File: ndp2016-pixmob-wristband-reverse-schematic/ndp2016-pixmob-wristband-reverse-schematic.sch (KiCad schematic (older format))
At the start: 18 parts, among them IC1 AT24C02S, IC2 MC81F4204_V/M/R, SW1 Single-Axis Accelerometer, U1 IR

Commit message: schematic
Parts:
- SW1: value Single-Axis Accelerometer -> Accelerometer
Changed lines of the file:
@@
 encoding utf-8
 Sheet 1 1
-Title ""
-Date ""
-Rev ""
+Title "NDP2016 Pixmob Wristband Reverse Engineered"
+Date "2016-08-10"
+Rev "1"
 Comp ""
 Comment1 ""
@@
 P 8850 4600
 F 0 "SW1" H 8850 4700 50  0000 C CNN
-F 1 "Single-Axis Accelerometer" H 8850 4500 50  0000 C CNN
+F 1 "Accelerometer" H 8850 4500 50  0000 C CNN
 F 2 "" H 8850 4600 50  0000 C CNN
 F 3 "" H 8850 4600 50  0000 C CNN

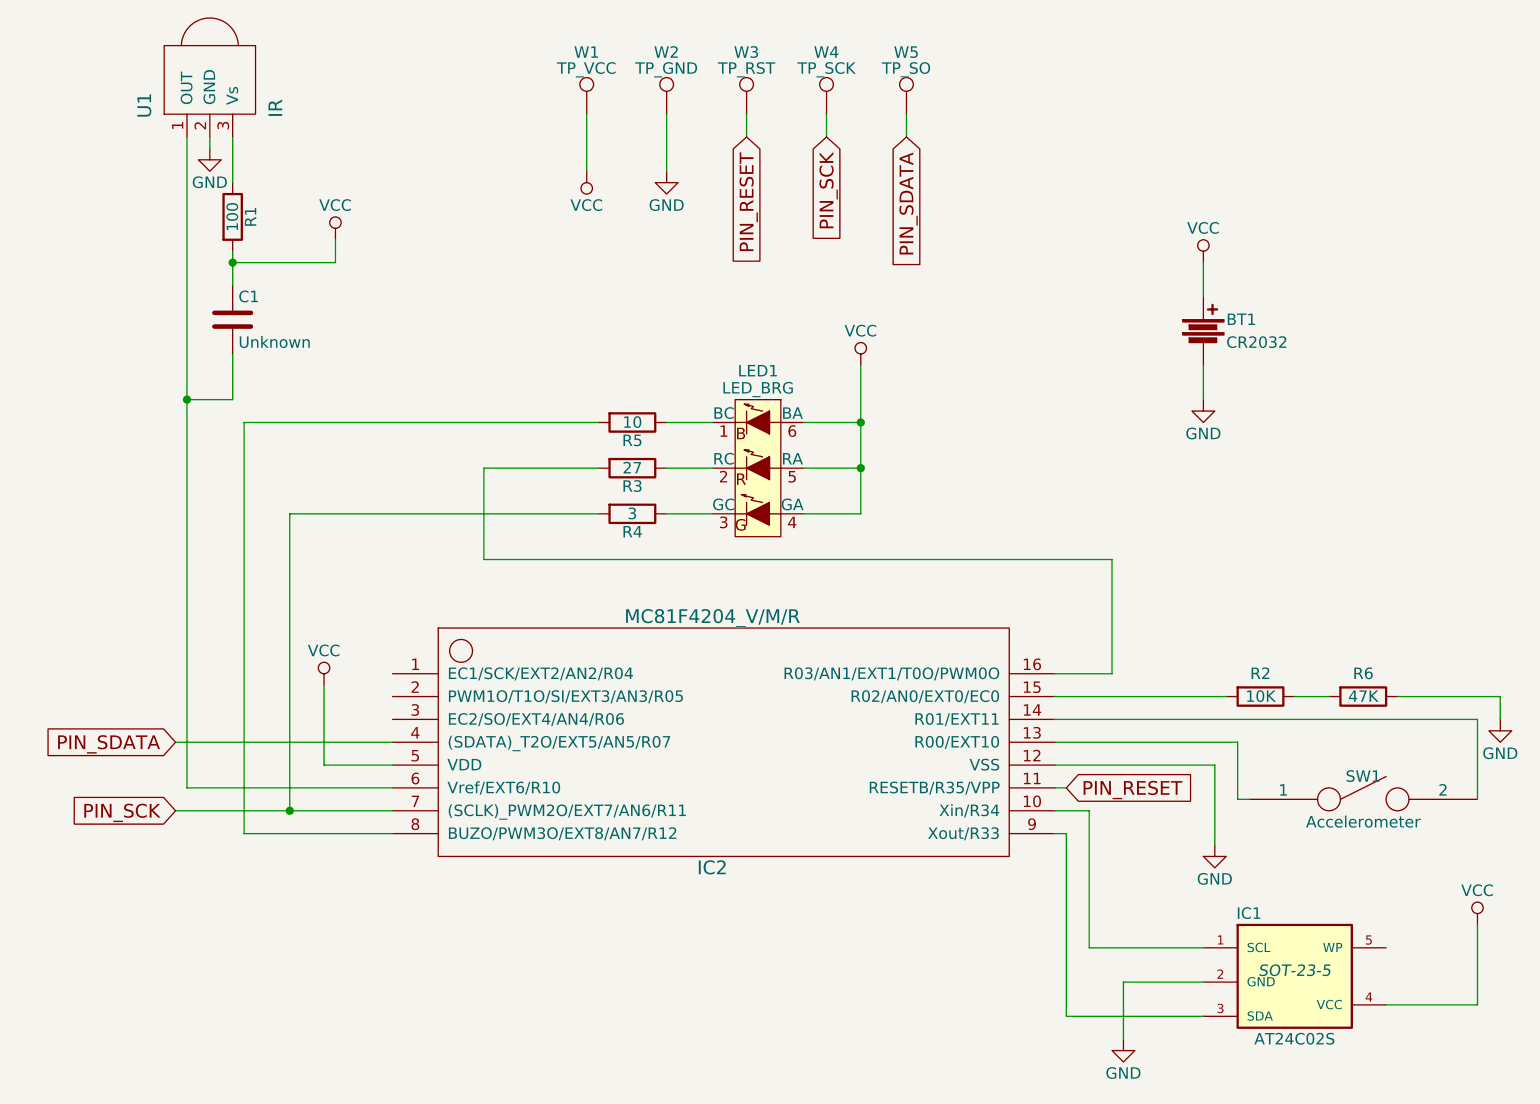
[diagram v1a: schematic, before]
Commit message: adjust cap ground
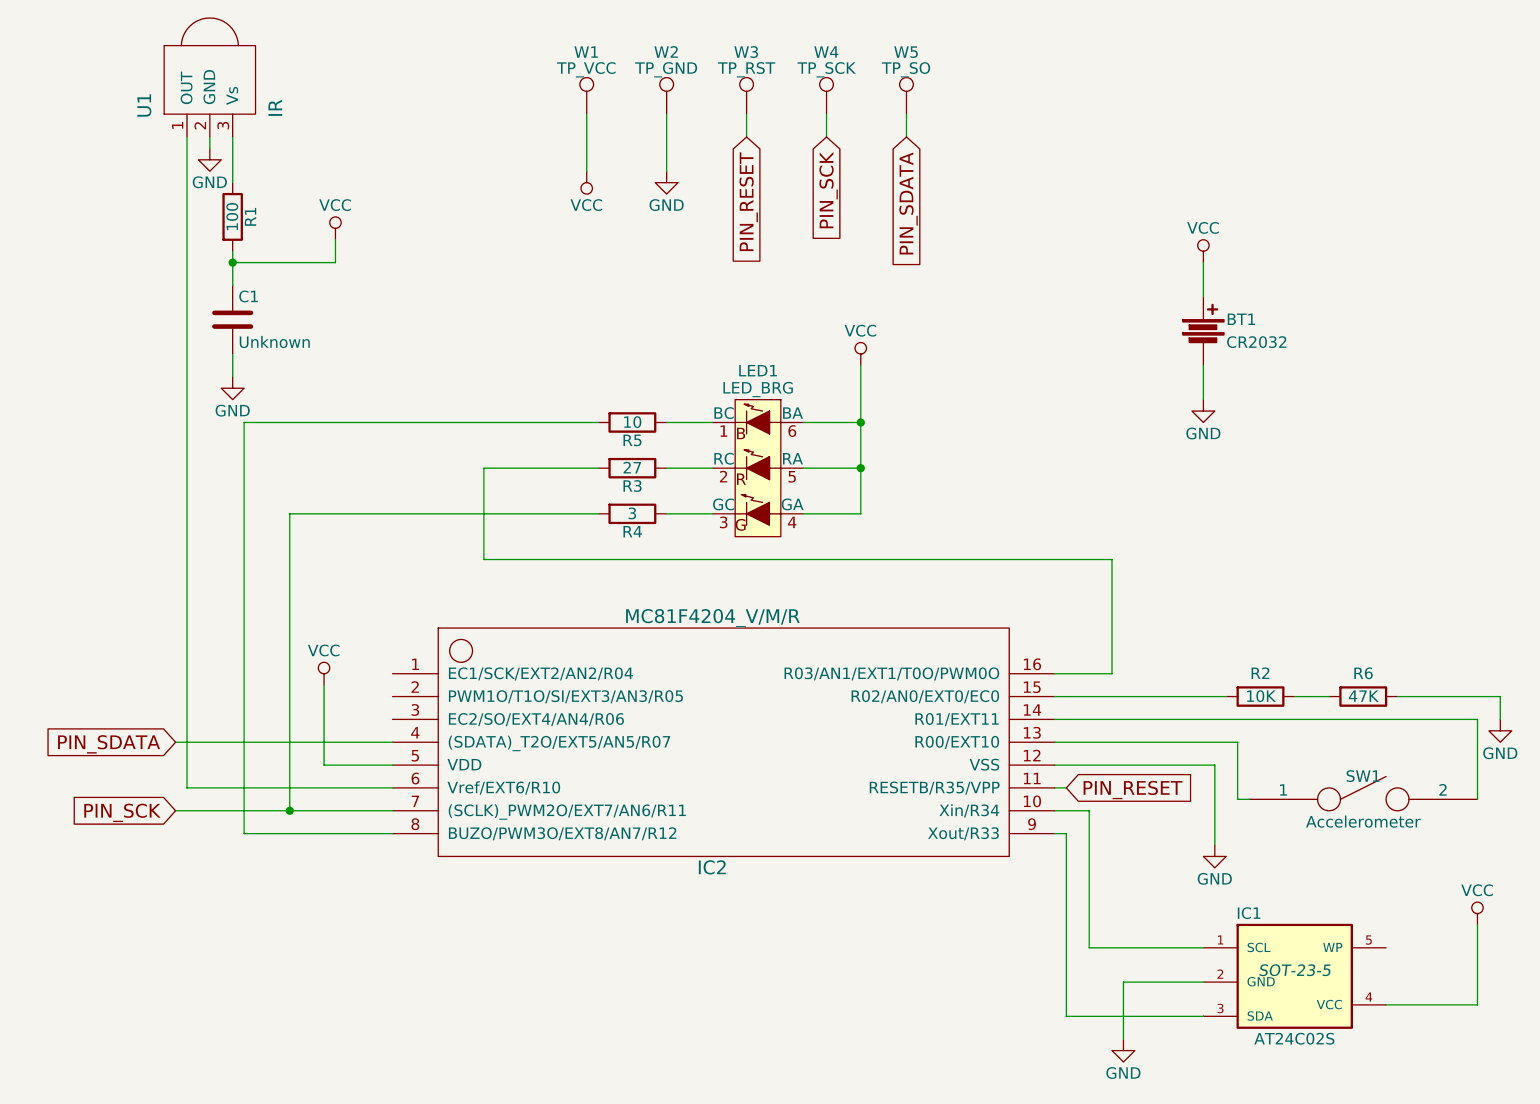
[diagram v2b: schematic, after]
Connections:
- net GND: now also C1.2
- net at IC2.6 (Vref/EXT6/R10), U1.1 (OUT): no longer C1.2
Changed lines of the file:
@@
 $EndComp
 Wire Wire Line
-	6650 2700 6650 2950
-Wire Wire Line
-	6650 2950 6650 3150
-Wire Wire Line
-	6650 3150 6650 3350
+	6650 2700 6650 3350
 Connection ~ 6650 2950
 Connection ~ 6650 3150
@@
 	3900 1700 3900 1900
 Wire Wire Line
-	3900 2200 3900 2250
-Wire Wire Line
-	3900 2250 3900 2350
+	3900 2200 3900 2350
 Wire Wire Line
 	3900 2250 4350 2250
@@
 	3700 4550 4600 4550
 Wire Wire Line
-	3700 1700 3700 2850
-Wire Wire Line
-	3700 2850 3700 4550
+	3700 1700 3700 4550
 Wire Wire Line
 	3950 2950 3950 4750
@@
 	4150 3350 4150 4650
 Wire Wire Line
-	3650 4650 4150 4650
-Wire Wire Line
-	4150 4650 4600 4650
+	3650 4650 4600 4650
 $Comp
 L C C1
@@
 	1    0    0    -1
 $EndComp
-Wire Wire Line
-	3900 2650 3900 2850
-Wire Wire Line
-	3900 2850 3700 2850
-Connection ~ 3700 2850
 Connection ~ 3900 2250
 $Comp
@@
 Wire Wire Line
 	4600 4350 3650 4350
+$Comp
+L GND #PWR?
+U 1 1 57AB4EC9
+P 3900 2750
+F 0 "#PWR?" H 3900 2500 50  0001 C CNN
+F 1 "GND" H 3900 2600 50  0000 C CNN
+F 2 "" H 3900 2750 50  0000 C CNN
+F 3 "" H 3900 2750 50  0000 C CNN
+	1    3900 2750
+	1    0    0    -1
+$EndComp
+Wire Wire Line
+	3900 2650 3900 2750
 $EndSCHEMATC

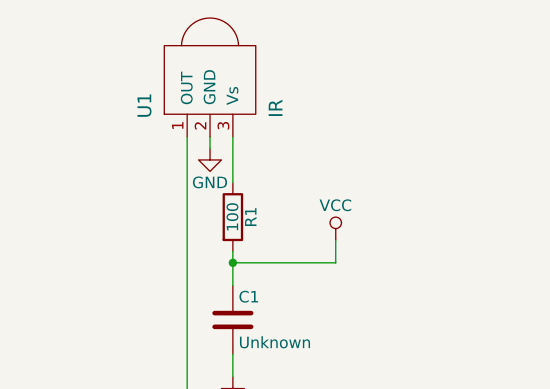
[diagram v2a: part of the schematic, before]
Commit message: adjust ir reference
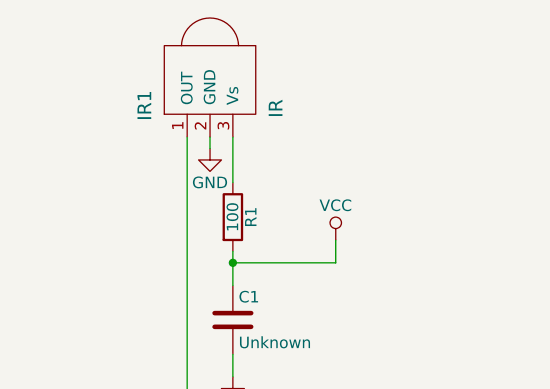
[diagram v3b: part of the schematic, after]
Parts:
- renumbered U1 to IR1
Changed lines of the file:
@@
 	6650 3350 6400 3350
 $Comp
-L IR U1
+L IR IR1
 U 1 1 57AAF6E0
 P 3800 1450
-F 0 "U1" H 3688 1735 60  0000 C CNN
+F 0 "IR1" H 3688 1735 60  0000 C CNN
 F 1 "IR" H 3675 1161 60  0000 C CNN
 F 2 "" H 3800 1450 60  0000 C CNN

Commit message: updated schematic
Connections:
- net GND: now also IC1.5 (WP), IC2.13 (R00/EXT10), SW1.1
- net VCC: now also R2.1, R6.2
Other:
- moved on the sheet: R2
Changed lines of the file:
@@
 	7500 4450 8200 4450
 Wire Wire Line
-	8200 4450 8200 4800
+	8200 4350 8200 4800
 $Comp
 L GND #PWR7
@@
 L R R2
 U 1 1 57AB2122
-P 8400 4150
-F 0 "R2" V 8300 4150 50  0000 C CNN
-F 1 "10K" V 8400 4150 50  0000 C CNN
-F 2 "" V 8330 4150 50  0000 C CNN
-F 3 "" H 8400 4150 50  0000 C CNN
-	1    8400 4150
+P 8100 4150
+F 0 "R2" V 8000 4150 50  0000 C CNN
+F 1 "10K" V 8100 4150 50  0000 C CNN
+F 2 "" V 8030 4150 50  0000 C CNN
+F 3 "" H 8100 4150 50  0000 C CNN
+	1    8100 4150
 	0    1    1    0
 $EndComp
@@
 	7500 4250 9350 4250
 Wire Wire Line
-	7500 4150 8250 4150
+	7500 4150 7950 4150
 $Comp
 L R R6
@@
 $EndComp
 Wire Wire Line
-	8550 4150 8700 4150
+	8250 4150 8700 4150
 Wire Wire Line
 	9000 4150 9450 4150
@@
 Wire Wire Line
 	3900 2650 3900 2750
+$Comp
+L VCC #PWR?
+U 1 1 57AC9CFC
+P 8500 3900
+F 0 "#PWR?" H 8500 3750 50  0001 C CNN
+F 1 "VCC" H 8500 4050 50  0000 C CNN
+F 2 "" H 8500 3900 50  0000 C CNN
+F 3 "" H 8500 3900 50  0000 C CNN
+	1    8500 3900
+	1    0    0    -1
+$EndComp
+Wire Wire Line
+	8500 4150 8500 3900
+Connection ~ 8500 4150
+$Comp
+L GND #PWR?
+U 1 1 57ACA1FC
+P 9050 5300
+F 0 "#PWR?" H 9050 5050 50  0001 C CNN
+F 1 "GND" H 9050 5150 50  0000 C CNN
+F 2 "" H 9050 5300 50  0000 C CNN
+F 3 "" H 9050 5300 50  0000 C CNN
+	1    9050 5300
+	1    0    0    -1
+$EndComp
+Wire Wire Line
+	8950 5250 9050 5250
+Wire Wire Line
+	9050 5250 9050 5300
+Connection ~ 8200 4350
+Connection ~ 8200 4450
 $EndSCHEMATC
